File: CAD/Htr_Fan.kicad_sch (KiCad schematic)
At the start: 49 parts, among them J29 V_OUT_6-9 Select, J52 V_OUT_3-5 Select, Q25 Q_DUAL_NMOS, Q26 Q_DUAL_NMOS, Q27 Q_DUAL_NMOS, U12 74HCT2G34GW,125, U8 74HCT365, U9 74HCT365

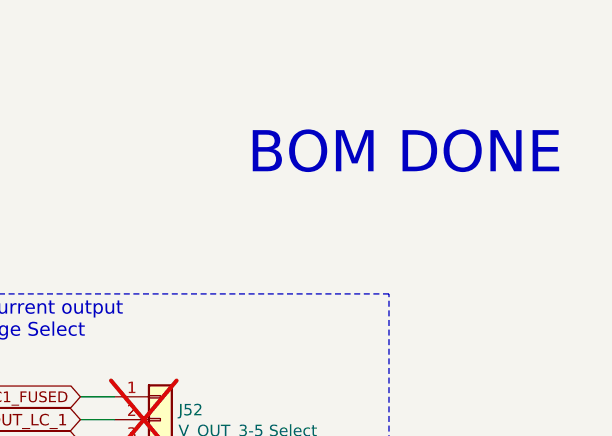
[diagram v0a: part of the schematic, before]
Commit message: WIP redoing board for new print
Removed version resistors.
Added pull-up on CMD.
Working on motors, not routed.
Added local library for custom parts.
Ran auto-cleanup of traces and vias (supervised).
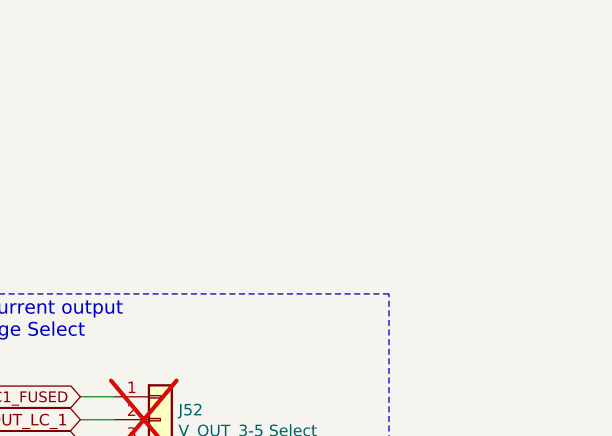
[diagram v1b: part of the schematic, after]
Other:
- note removed: "BOM DONE"
- company: Duet3d -> 3DPotter
- title: Duet 3 Main Board 6XD -> Duet 3 Main Board 3DP

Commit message: Pin Changes / Misc
Changing some pins around so I have a chip select
Processor Pins:
PC28 ---> PA9 (Driver_2_Step)
PC29[AFE1_AD4] ---> PB1[AFE1_AD0] (TEMP_1)
PC28 -> spi1cs1
PC29 -> spi1cs2 (Unused as of now)
IDC Header:
CAN 0 Lines removed
13 -> SPI1_MOSI_BUFF
14 -> SP1_MISO
18 -> SPI1_SPCK_BUFF
19 -> spi1cs1
Misc:
Fixed all library links, should get a lot less errors now
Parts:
- C74: footprint Capacitor_SMD:C_0402_1005Metric_Wbry -> Capacitor_SMD:C_0402_1005Metric
- R53: footprint Resistor_SMD:R_0402_1005Metric_Wbry -> Resistor_SMD:R_0402_1005Metric
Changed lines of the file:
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@@
 			)
 		)
-		(property "Footprint" "Resistor_SMD:R_0402_1005Metric_Wbry"
+		(property "Footprint" "Resistor_SMD:R_0402_1005Metric"
 			(at 156.21 255.27 0)
 			(effects
@@
 			)
 		)
-		(property "Footprint" "Capacitor_SMD:C_0402_1005Metric_Wbry"
+		(property "Footprint" "Capacitor_SMD:C_0402_1005Metric"
 			(at 207.01 215.9 0)
 			(effects

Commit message: V1.55 Pre Maufacturing
Final change for 1.55, changed connectors to jst due to board height issues with the stepper boards
DFM passed
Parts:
- C74, R53, U9: now not fitted; now left out of the parts list
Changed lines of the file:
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@@
 	(title_block
 		(title "Duet 3 Main Board 3DP")
-		(date "2023-02-22")
-		(rev "1.5")
+		(date "2026-02-17")
+		(rev "1.55")
 		(company "3DPotter")
 		(comment 1 "(c) 3DPotter")
@@
 		(unit 1)
 		(exclude_from_sim no)
-		(in_bom yes)
-		(on_board yes)
-		(dnp no)
+		(in_bom no)
+		(on_board no)
+		(dnp yes)
 		(property "Reference" "R53"
 			(at 154.305 255.4732 90)
@@
 		(unit 1)
 		(exclude_from_sim no)
-		(in_bom yes)
-		(on_board yes)
-		(dnp no)
+		(in_bom no)
+		(on_board no)
+		(dnp yes)
 		(property "Reference" "C74"
 			(at 208.915 218.44 90)
@@
 		(unit 1)
 		(exclude_from_sim no)
-		(in_bom yes)
-		(on_board yes)
-		(dnp no)
+		(in_bom no)
+		(on_board no)
+		(dnp yes)
 		(property "Reference" "#PWR066"
 			(at 213.36 220.98 0)
@@
 		(unit 1)
 		(exclude_from_sim no)
-		(in_bom yes)
-		(on_board yes)
-		(dnp no)
+		(in_bom no)
+		(on_board no)
+		(dnp yes)
 		(property "Reference" "U9"
 			(at 195.58 234.95 0)

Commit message: Finalize changes for 1.56
LCSC and P/N updated for excessively out of stock parts.
Silkscreen changes so no more DRC errors
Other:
- title: Duet 3 Main Board 3DP -> Duet 3 MB 3DP
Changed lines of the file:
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@@
 	(paper "A3" portrait)
 	(title_block
-		(title "Duet 3 Main Board 3DP")
-		(date "2026-02-17")
-		(rev "1.55")
+		(title "Duet 3 MB 3DP")
+		(date "2026-06-02")
+		(rev "1.56")
 		(company "3DPotter")
 		(comment 1 "(c) 3DPotter")
